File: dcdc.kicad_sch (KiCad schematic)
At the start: 198 parts, among them U11 SIC431AED-T1-GE3, U12 SIC431AED-T1-GE3, U13 SIC431AED-T1-GE3, U22 INA219AIDCNR, U50 INA219AIDCNR, U60 INA219AIDCNR, U65 SIC431AED-T1-GE3, U66 INA219AIDCNR, U69 TPS564247DRLR, U7 TPS564247DRLR, U75 SIC431AED-T1-GE3, U76 INA219AIDCNR, U8 SIC431AED-T1-GE3

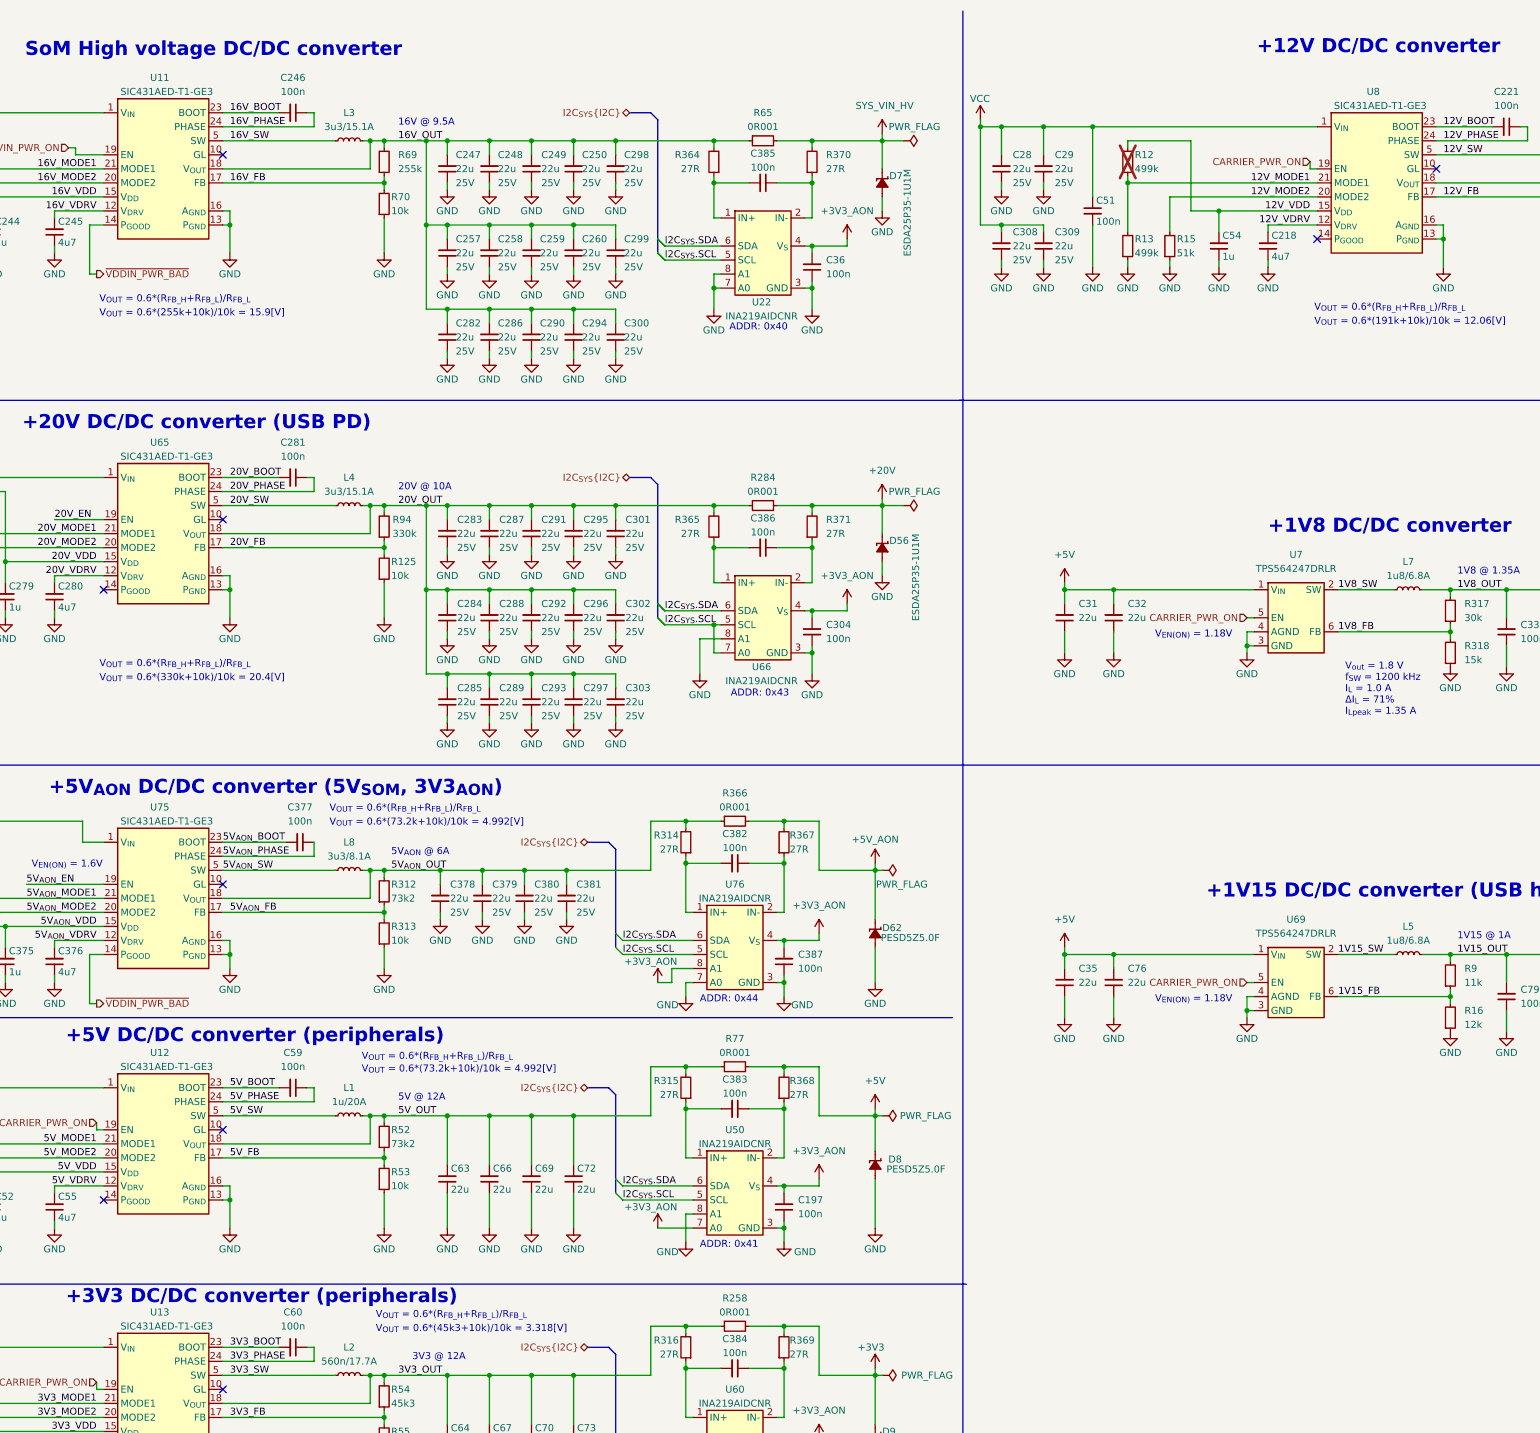
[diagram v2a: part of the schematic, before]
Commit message: [#90855] Replace SIC431AED-T1-GE3 dc-dc ICs with SIC437AED-T1-GE3
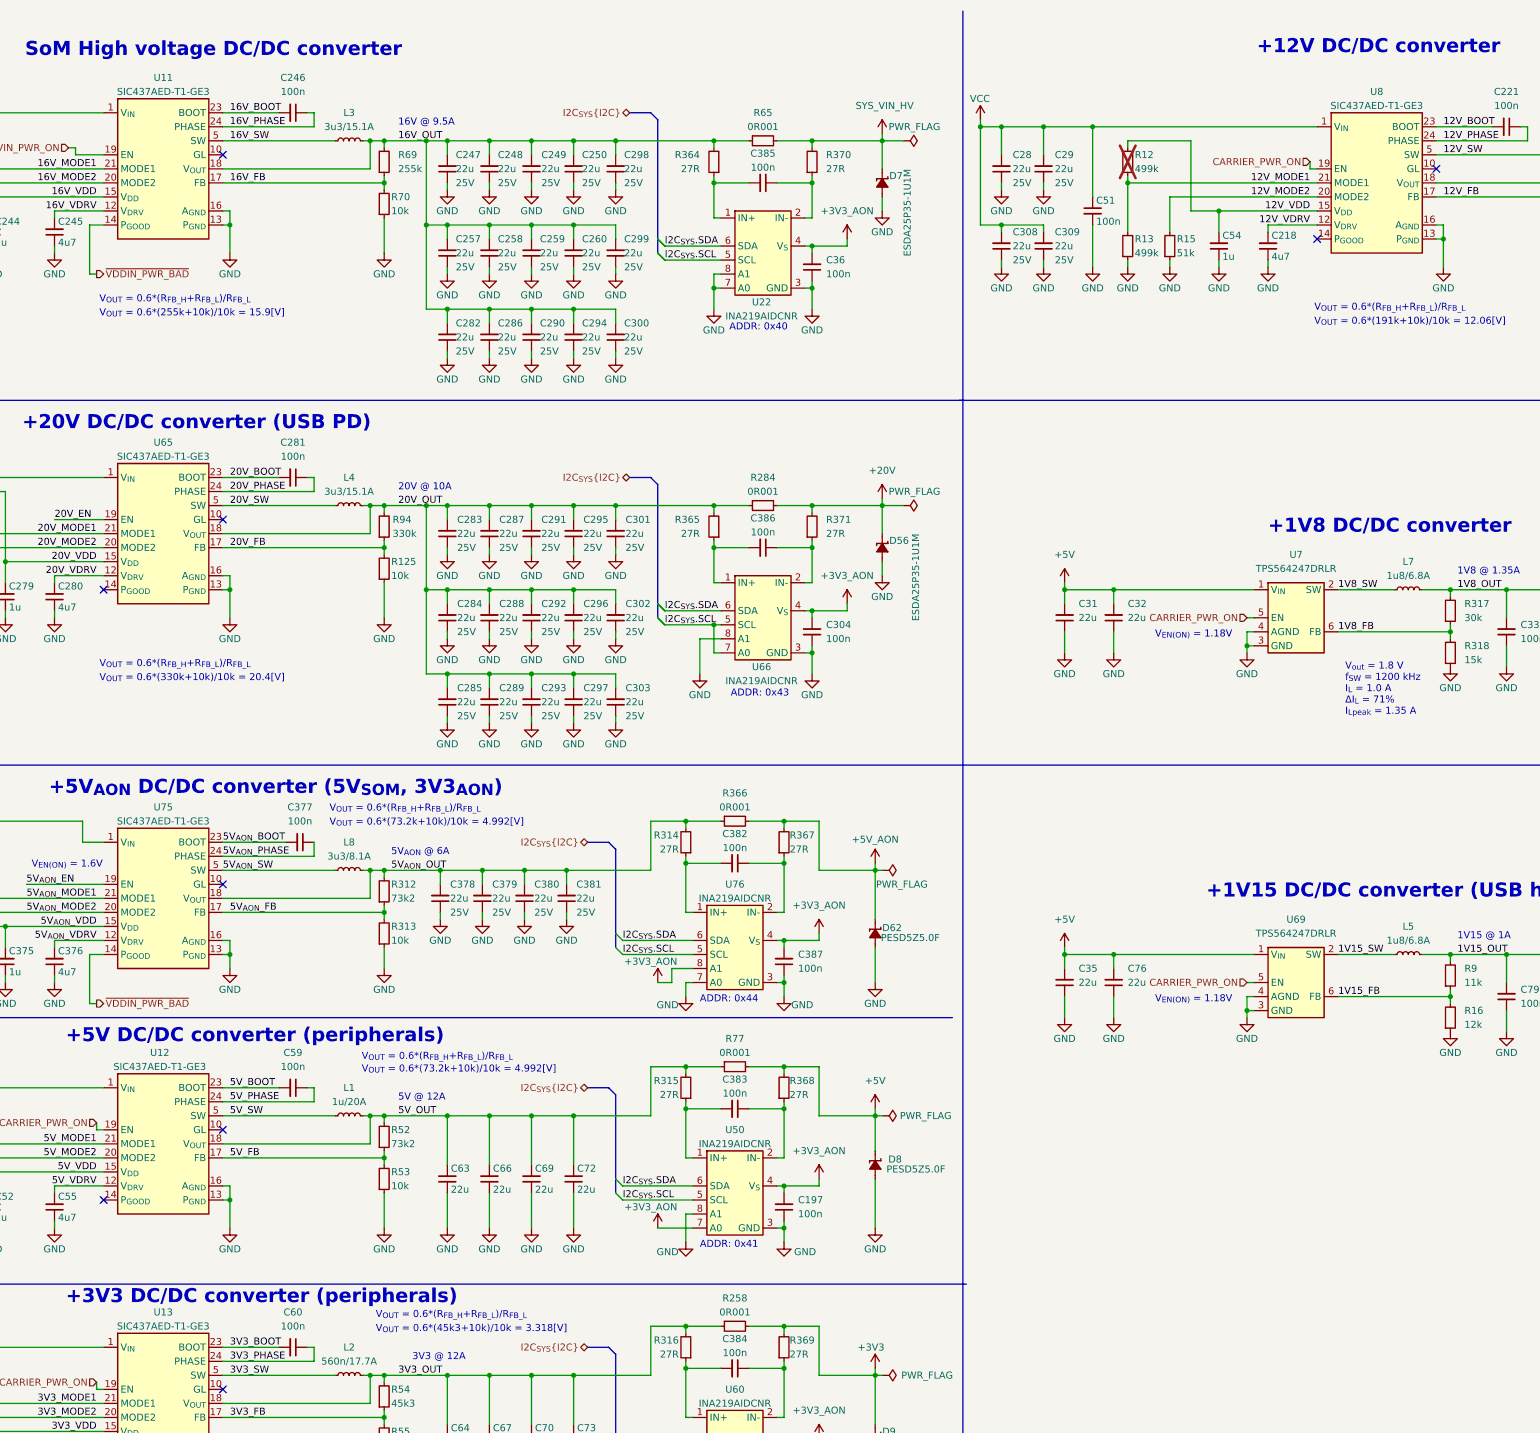
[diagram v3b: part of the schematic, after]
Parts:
- U11, U12, U13, U65, U75, U8: value SIC431AED-T1-GE3 -> SIC437AED-T1-GE3; symbol antmicroDCDCConverters:SIC431AED-T1-GE3 -> antmicroDCDCConverters:SIC437AED-T1-GE3; MPN SIC431AED-T1-GE3 -> SIC437AED-T1-GE3
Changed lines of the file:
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@@
 	)
 	(symbol
-		(lib_id "antmicroDCDCConverters:SIC431AED-T1-GE3")
+		(lib_id "antmicroDCDCConverters:SIC437AED-T1-GE3")
 		(at 92.71 96.52 0)
 		(unit 1)
@@
 		(dnp no)
 		(property "Reference" "U65"
-			(at 102.87 90.17 0)
+			(at 103.505 90.17 0)
 			(effects
 				(font
@@
 			)
 		)
-		(property "Value" "SIC431AED-T1-GE3"
+		(property "Value" "SIC437AED-T1-GE3"
 			(at 125.73 104.14 0)
 			(effects
@@
 			)
 		)
-		(property "Datasheet" "https://www.vishay.com/docs/74589/sic431.pdf"
+		(property "Datasheet" "https://www.vishay.com/docs/75921/sic437.pdf"
 			(at 125.73 109.22 0)
 			(effects
@@
 			)
 		)
-		(property "Description" "DC/DC Synchronous Regulator, Adjustable, 3V to 24VIn, 0.6V to 22V/24AOut, 1MHz, MLP44-24L"
-			(at 92.71 96.52 0)
+		(property "Description" "DC/DC Buck Step Down Regulator Adjustable, 4.5-28V In, 0.6V to 20V/12A Out, 1MHz, PowerPAK MLP44-24"
+			(at 125.73 119.38 0)
 			(effects
 				(font
 					(size 1.27 1.27)
 				)
+				(justify left bottom)
 				(hide yes)
 			)
@@
 			)
 		)
-		(property "MPN" "SIC431AED-T1-GE3 "
-			(at 104.14 92.71 0)
+		(property "MPN" "SIC437AED-T1-GE3"
+			(at 103.505 92.71 0)
 			(effects
 				(font
@@
 	)
 	(symbol
-		(lib_id "antmicroDCDCConverters:SIC431AED-T1-GE3")
+		(lib_id "antmicroDCDCConverters:SIC437AED-T1-GE3")
 		(at 92.71 162.56 0)
 		(unit 1)
@@
 		(dnp no)
 		(property "Reference" "U75"
-			(at 102.87 156.21 0)
+			(at 103.505 156.21 0)
 			(effects
 				(font
@@
 			)
 		)
-		(property "Value" "SIC431AED-T1-GE3"
+		(property "Value" "SIC437AED-T1-GE3"
 			(at 125.73 170.18 0)
 			(effects
@@
 			)
 		)
-		(property "Datasheet" "https://www.vishay.com/docs/74589/sic431.pdf"
+		(property "Datasheet" "https://www.vishay.com/docs/75921/sic437.pdf"
 			(at 125.73 175.26 0)
 			(effects
@@
 			)
 		)
-		(property "Description" "DC/DC Synchronous Regulator, Adjustable, 3V to 24VIn, 0.6V to 22V/24AOut, 1MHz, MLP44-24L"
-			(at 92.71 162.56 0)
+		(property "Description" "DC/DC Buck Step Down Regulator Adjustable, 4.5-28V In, 0.6V to 20V/12A Out, 1MHz, PowerPAK MLP44-24"
+			(at 125.73 185.42 0)
 			(effects
 				(font
 					(size 1.27 1.27)
 				)
+				(justify left bottom)
 				(hide yes)
 			)
@@
 			)
 		)
-		(property "MPN" "SIC431AED-T1-GE3 "
-			(at 104.14 158.75 0)
+		(property "MPN" "SIC437AED-T1-GE3"
+			(at 103.505 158.75 0)
 			(effects
 				(font
@@
 	)
 	(symbol
-		(lib_id "antmicroDCDCConverters:SIC431AED-T1-GE3")
+		(lib_id "antmicroDCDCConverters:SIC437AED-T1-GE3")
 		(at 92.71 207.01 0)
 		(unit 1)
@@
 			)
 		)
-		(property "Value" "SIC431AED-T1-GE3"
+		(property "Value" "SIC437AED-T1-GE3"
 			(at 125.73 214.63 0)
 			(effects
@@
 			)
 		)
-		(property "Datasheet" "https://www.vishay.com/docs/74589/sic431.pdf"
+		(property "Datasheet" "https://www.vishay.com/docs/75921/sic437.pdf"
 			(at 125.73 219.71 0)
 			(effects
@@
 			)
 		)
-		(property "Description" "DC/DC Synchronous Regulator, Adjustable, 3V to 24VIn, 0.6V to 22V/24AOut, 1MHz, MLP44-24L"
-			(at 92.71 207.01 0)
+		(property "Description" "DC/DC Buck Step Down Regulator Adjustable, 4.5-28V In, 0.6V to 20V/12A Out, 1MHz, PowerPAK MLP44-24"
+			(at 125.73 229.87 0)
 			(effects
 				(font
 					(size 1.27 1.27)
 				)
+				(justify left bottom)
 				(hide yes)
 			)
@@
 			)
 		)
-		(property "MPN" "SIC431AED-T1-GE3 "
-			(at 104.14 203.2 0)
+		(property "MPN" "SIC437AED-T1-GE3"
+			(at 102.87 203.2 0)
 			(effects
 				(font
@@
 	)
 	(symbol
-		(lib_id "antmicroDCDCConverters:SIC431AED-T1-GE3")
+		(lib_id "antmicroDCDCConverters:SIC437AED-T1-GE3")
 		(at 92.71 30.48 0)
 		(unit 1)
@@
 		(dnp no)
 		(property "Reference" "U11"
-			(at 102.87 24.13 0)
+			(at 103.505 24.13 0)
 			(effects
 				(font
@@
 			)
 		)
-		(property "Value" "SIC431AED-T1-GE3"
+		(property "Value" "SIC437AED-T1-GE3"
 			(at 125.73 38.1 0)
 			(effects
@@
 			)
 		)
-		(property "Datasheet" "https://www.vishay.com/docs/74589/sic431.pdf"
+		(property "Datasheet" "https://www.vishay.com/docs/75921/sic437.pdf"
 			(at 125.73 43.18 0)
 			(effects
@@
 			)
 		)
-		(property "Description" "DC/DC Synchronous Regulator, Adjustable, 3V to 24VIn, 0.6V to 22V/24AOut, 1MHz, MLP44-24L"
-			(at 92.71 30.48 0)
+		(property "Description" "DC/DC Buck Step Down Regulator Adjustable, 4.5-28V In, 0.6V to 20V/12A Out, 1MHz, PowerPAK MLP44-24"
+			(at 125.73 53.34 0)
 			(effects
 				(font
 					(size 1.27 1.27)
 				)
+				(justify left bottom)
 				(hide yes)
 			)
@@
 			)
 		)
-		(property "MPN" "SIC431AED-T1-GE3 "
-			(at 104.14 26.67 0)
+		(property "MPN" "SIC437AED-T1-GE3"
+			(at 103.505 26.67 0)
 			(effects
 				(font
@@
 	)
 	(symbol
-		(lib_id "antmicroDCDCConverters:SIC431AED-T1-GE3")
+		(lib_id "antmicroDCDCConverters:SIC437AED-T1-GE3")
 		(at 312.42 33.02 0)
 		(unit 1)
@@
 		(dnp no)
 		(property "Reference" "U8"
-			(at 322.58 26.67 0)
+			(at 323.215 26.67 0)
 			(effects
 				(font
@@
 			)
 		)
-		(property "Value" "SIC431AED-T1-GE3"
+		(property "Value" "SIC437AED-T1-GE3"
 			(at 345.44 40.64 0)
 			(effects
@@
 			)
 		)
-		(property "Datasheet" "https://www.vishay.com/docs/74589/sic431.pdf"
+		(property "Datasheet" "https://www.vishay.com/docs/75921/sic437.pdf"
 			(at 345.44 45.72 0)
 			(effects
@@
 			)
 		)
-		(property "Description" "DC/DC Synchronous Regulator, Adjustable, 3V to 24VIn, 0.6V to 22V/24AOut, 1MHz, MLP44-24L"
-			(at 312.42 33.02 0)
+		(property "Description" "DC/DC Buck Step Down Regulator Adjustable, 4.5-28V In, 0.6V to 20V/12A Out, 1MHz, PowerPAK MLP44-24"
+			(at 345.44 55.88 0)
 			(effects
 				(font
 					(size 1.27 1.27)
 				)
+				(justify left bottom)
 				(hide yes)
 			)
@@
 			)
 		)
-		(property "MPN" "SIC431AED-T1-GE3 "
-			(at 323.85 29.21 0)
+		(property "MPN" "SIC437AED-T1-GE3"
+			(at 323.215 29.21 0)
 			(effects
 				(font
@@
 	)
 	(symbol
-		(lib_id "antmicroDCDCConverters:SIC431AED-T1-GE3")
+		(lib_id "antmicroDCDCConverters:SIC437AED-T1-GE3")
 		(at 92.71 254 0)
 		(unit 1)
@@
 		(dnp no)
 		(property "Reference" "U13"
-			(at 102.87 247.65 0)
+			(at 103.505 247.65 0)
 			(effects
 				(font
@@
 			)
 		)
-		(property "Value" "SIC431AED-T1-GE3"
+		(property "Value" "SIC437AED-T1-GE3"
 			(at 125.73 261.62 0)
 			(effects
@@
 			)
 		)
-		(property "Datasheet" "https://www.vishay.com/docs/74589/sic431.pdf"
+		(property "Datasheet" "https://www.vishay.com/docs/75921/sic437.pdf"
 			(at 125.73 266.7 0)
 			(effects
@@
 			)
 		)
-		(property "Description" "DC/DC Synchronous Regulator, Adjustable, 3V to 24VIn, 0.6V to 22V/24AOut, 1MHz, MLP44-24L"
-			(at 92.71 254 0)
+		(property "Description" "DC/DC Buck Step Down Regulator Adjustable, 4.5-28V In, 0.6V to 20V/12A Out, 1MHz, PowerPAK MLP44-24"
+			(at 125.73 276.86 0)
 			(effects
 				(font
 					(size 1.27 1.27)
 				)
+				(justify left bottom)
 				(hide yes)
 			)
@@
 			)
 		)
-		(property "MPN" "SIC431AED-T1-GE3 "
-			(at 104.14 250.19 0)
+		(property "MPN" "SIC437AED-T1-GE3"
+			(at 103.505 250.19 0)
 			(effects
 				(font
